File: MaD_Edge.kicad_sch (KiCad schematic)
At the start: 15 parts

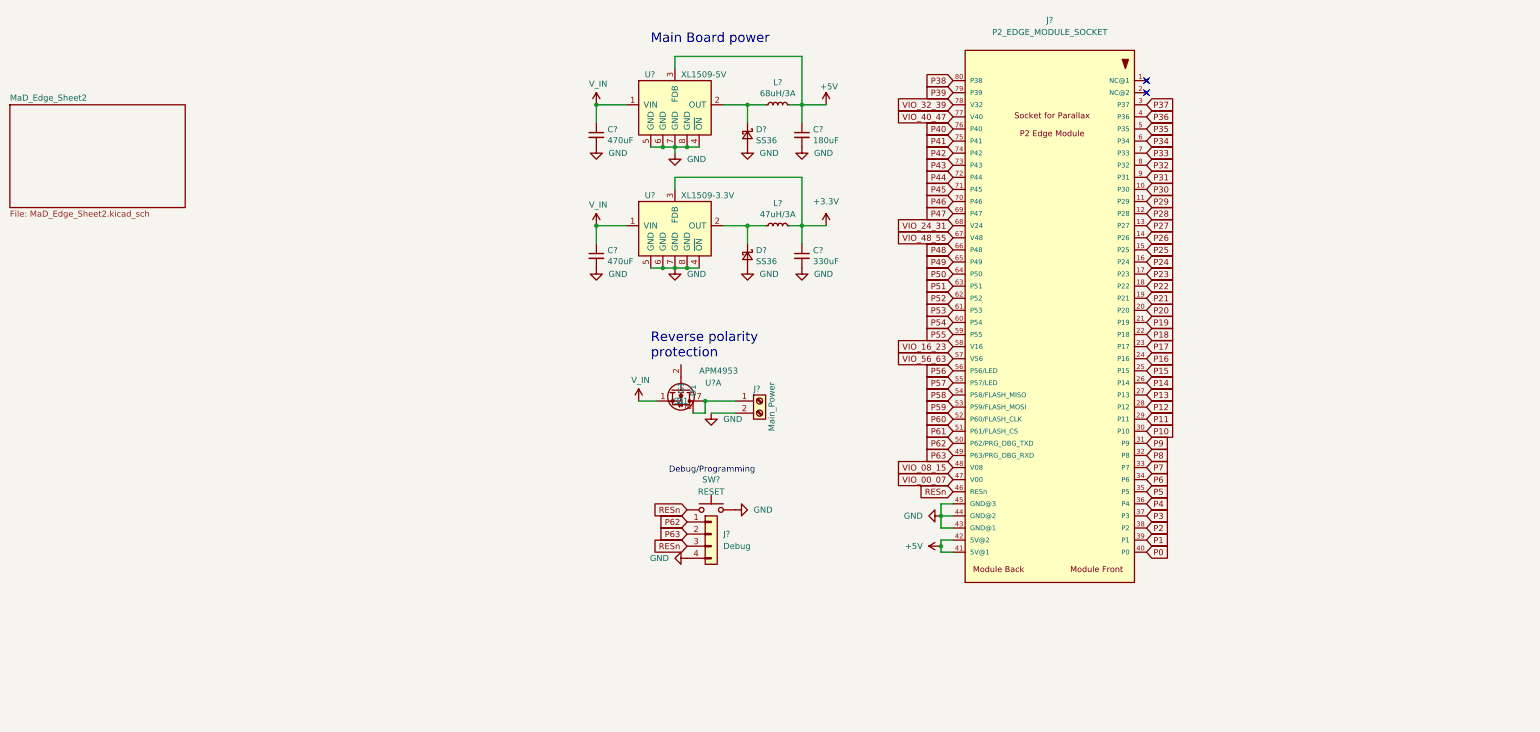
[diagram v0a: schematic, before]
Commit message: new Mad Edge being manufactured
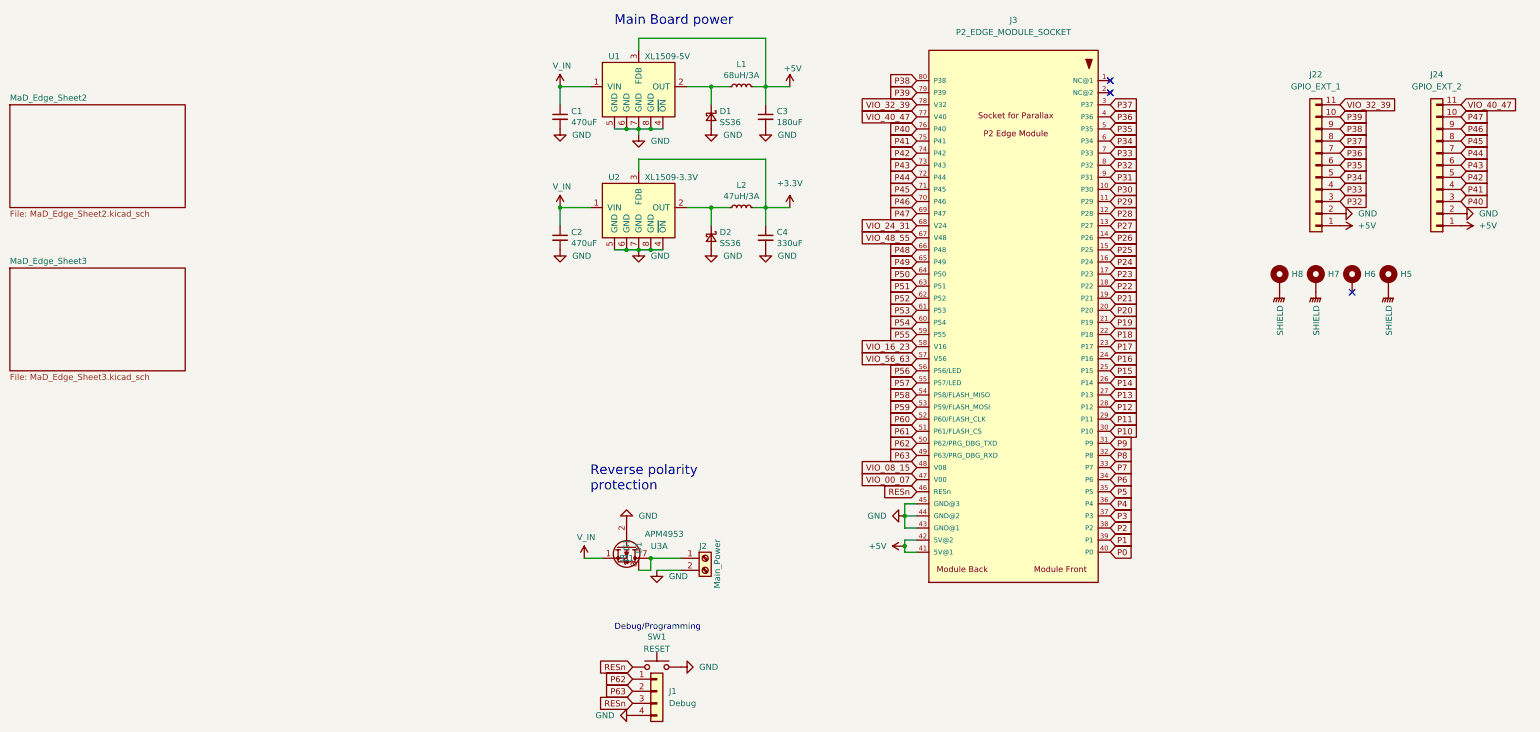
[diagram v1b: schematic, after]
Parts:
- added H5, H6, H7, H8: MountingHole_Pad, MountingHole:MountingHole_4mm_Pad, symbol Mechanical:MountingHole_Pad
- added J22: GPIO_EXT_1, Connector_PinHeader_1.27mm:PinHeader_1x11_P1.27mm_Vertical, symbol Connector_Generic:Conn_01x11
- added J24: GPIO_EXT_2, Connector_PinHeader_1.27mm:PinHeader_1x11_P1.27mm_Vertical, symbol Connector_Generic:Conn_01x11
- C1, C2: renamed from C?; footprint (none) -> Capacitor_SMD:C_Elec_10x10.2; DIGIKEY 399-18277-1-ND -> 10-EEH-ZS1E471PCT-ND; Height (none) -> 12.80mm; LCSC (none) -> C3350; MANUFACTURER (none) -> Panasonic Electronic Components; Manufacturer_Part_Number (none) -> EEH-ZS1E471P; Type NA -> (none); manufacturer_1 (none) -> Honor Elec; manufacturer_part_number_1 (none) -> RVT1V471M1010
- C3: renamed from C?; footprint (none) -> Capacitor_SMD:CP_Elec_8x6.9; DIGIKEY 1189-2158-ND -> P16510CT-ND; Height (none) -> 12.00mm; LCSC (none) -> C413657; MANUFACTURER (none) -> Panasonic Electronic Components; Manufacturer_Part_Number (none) -> 25SVPF180M; Type NA -> (none); manufacturer_1 (none) -> PANASONIC; manufacturer_part_number_1 (none) -> EEEFKE181XSP
- C4: renamed from C?; footprint (none) -> Capacitor_SMD:C_Elec_10x10.2; DIGIKEY 493-11736-1-ND -> P16512CT-ND; Height (none) -> 12.70mm; LCSC (none) -> C5155335; MANUFACTURER (none) -> Panasonic Electronic Components; Manufacturer_Part_Number (none) -> 25SVPF330M; Type NA -> (none); manufacturer_1 (none) -> KNSCHA; manufacturer_part_number_1 (none) -> LZ330UF35V90RV0141
- D1, D2: renamed from D?; footprint (none) -> Diode_SMD:D_SMC; DIGIKEY (none) -> SS36-E3/57TGICT-ND; MANUFACTURER (none) -> Vishay General Semiconductor - Diodes Division; Manufacturer_Part_Number (none) -> SS36-E3/57T; Type BASIC -> (none); manufacturer_1 (none) -> Vishay Intertech; manufacturer_part_number_1 (none) -> SS36-E3/57T
- J1: renamed from J?; footprint (none) -> Connector_PinHeader_2.54mm:PinHeader_1x04_P2.54mm_Vertical; LCSC (none) -> DNP; MANUFACTURER (none) -> DNP; Manufacturer_Part_Number (none) -> DNP; manufacturer_1 (none) -> DNP; manufacturer_part_number_1 (none) -> DNP
- J2: renamed from J?; footprint TerminalBlock:TerminalBlock_bornier-2_P5.08mm -> 70553-0106:705530106; DIGIKEY (none) -> WM4153-ND; LCSC (none) -> C239384; MANUFACTURER (none) -> Molex; Manufacturer_Part_Number (none) -> 0705530106; Type NA -> (none); manufacturer_1 (none) -> CJT(Changjiang Connectors); manufacturer_part_number_1 (none) -> A2547WR-2P
- J3: renamed from J?; footprint P2_EDGE_MODULE_SOCKET:Card_Edge_TH_VERT_1.27mm_80p -> P2_EDGE_MODULE_SOCKET:Card_Edge_SMT_VERT_1.27mm_80p; LCSC (none) -> DNP; Manufacturer_Part_Number (none) -> 450-00309; manufacturer_1 (none) -> DNP; manufacturer_part_number_1 (none) -> DNP
- L1: renamed from L?; footprint (none) -> Inductor_SMD:L_10.4x10.4_H4.8; DIGIKEY (none) -> SRP1038A-470MCT-ND; Height (none) -> 4.00mm; LCSC C497902 -> C408492; MANUFACTURER (none) -> Bourns Inc.; Manufacturer_Part_Number (none) -> SRP1038A-470M; Type EXT -> (none); manufacturer_1 (none) -> Sunlord; manufacturer_part_number_1 (none) -> MWSA1004S-680MT
- L2: renamed from L?; footprint (none) -> Inductor_SMD:L_10.4x10.4_H4.8; LCSC C115409 -> C149548; MANUFACTURER (none) -> Sunltech Tech; Manufacturer_Part_Number (none) -> SLO1365H470MTT; Type EXT -> (none); manufacturer_1 (none) -> SXN(Shun Xiang Nuo Elec); manufacturer_part_number_1 (none) -> SMMS1050-470M
- SW1: renamed from SW?; footprint (none) -> Button_Switch_SMD:SW_SPST_PTS645; LCSC (none) -> C2804591; manufacturer_1 (none) -> C&K; manufacturer_part_number_1 (none) -> PTS645VK31LFS
- U1: renamed from U?; footprint (none) -> Package_SO:SOP-8_3.9x4.9mm_P1.27mm; MANUFACTURER (none) -> XLSEMI; Manufacturer_Part_Number (none) -> XL1509-5.0E1; Type BASIC -> (none); manufacturer_1 (none) -> XLSEMI; manufacturer_part_number_1 (none) -> XL1509-5.0E1
- U2: renamed from U?; footprint (none) -> Package_SO:SOP-8_3.9x4.9mm_P1.27mm; LCSC C74193 -> C74193; MANUFACTURER (none) -> XLSEMI; Manufacturer_Part_Number (none) -> XL1509-3.3E1; Type EXT -> (none); manufacturer_1 (none) -> XLSEMI; manufacturer_part_number_1 (none) -> XL1509-3.3E1
- U3: renamed from U?; MANUFACTURER (none) -> Anpec Elec; Manufacturer_Part_Number (none) -> APM4953KC-TRG; Type BASIC -> (none); manufacturer_1 (none) -> Anpec Elec; manufacturer_part_number_1 (none) -> APM4953KC-TRG
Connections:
- net +5V: now also J22.1 (Pin_1), J24.1 (Pin_1)
- net GND: now also U3.2 (G1), J22.2 (Pin_2), J24.2 (Pin_2)
- net P32: now also J22.3 (Pin_3)
- net P33: now also J22.4 (Pin_4)
- net P34: now also J22.5 (Pin_5)
- net P35: now also J22.6 (Pin_6)
- net P36: now also J22.7 (Pin_7)
- net P37: now also J22.8 (Pin_8)
- net P38: now also J22.9 (Pin_9)
- net P39: now also J22.10 (Pin_10)
- net P40: now also J24.3 (Pin_3)
- net P41: now also J24.4 (Pin_4)
- net P42: now also J24.5 (Pin_5)
- net P43: now also J24.6 (Pin_6)
- net P44: now also J24.7 (Pin_7)
- net P45: now also J24.8 (Pin_8)
- net P46: now also J24.9 (Pin_9)
- net P47: now also J24.10 (Pin_10)
- net VIO_32_39: now also J22.11 (Pin_11)
- net VIO_40_47: now also J24.11 (Pin_11)
- new net SHIELD: H5.1, H7.1, H8.1
- no-connect marks 2 -> 3
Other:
- added sheet MaD_Edge_Sheet3 (MaD_Edge_Sheet3.kicad_sch)
- moved on the sheet: C1, C2, C3, C4, D1, D2, J1, J2, J3, L1, L2, SW1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

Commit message: working version for getting basic data for the thesis
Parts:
- C1, C2, D1, D2: Qty Bought (none) -> 10 - lcsc
- C3, C4, L2, U1, U2, U3: Qty Bought (none) -> 5 - lcsc
- H5, H6, H7, H8, J1, J22, J24, J3, SW1: Qty Bought (none) -> NA
- J2: LCSC C239384 -> C5333422; Qty Bought (none) -> 4 - lcsc
- L1: Qty Bought (none) -> 5 -lcsc
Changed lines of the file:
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@@
       (effects (font (size 1.27 1.27)) hide)
     )
-    (property "LCSC" "C239384" (at 107.95 142.24 0)
+    (property "LCSC" "C5333422" (at 107.95 142.24 0)
       (effects (font (size 1.27 1.27)) hide)
     )
@@
     )
     (property "manufacturer_part_number_1" "A2547WR-2P" (at 107.95 142.24 0)
+      (effects (font (size 1.27 1.27)) hide)
+    )
+    (property "Qty Bought" "4 - lcsc" (at 107.95 142.24 0)
+      (effects (font (size 1.27 1.27)) hide)
+    )
+    (property "Receptical" "" (at 107.95 142.24 0)
       (effects (font (size 1.27 1.27)) hide)
     )
@@
       (effects (font (size 1.27 1.27)) hide)
     )
+    (property "Qty Bought" "NA" (at 251.46 83.82 0)
+      (effects (font (size 1.27 1.27)) hide)
+    )
+    (property "Receptical" "" (at 251.46 83.82 0)
+      (effects (font (size 1.27 1.27)) hide)
+    )
     (pin "1")
     (instances
@@
       (effects (font (size 1.27 1.27)) hide)
     )
+    (property "Qty Bought" "NA" (at 228.6 83.82 0)
+      (effects (font (size 1.27 1.27)) hide)
+    )
+    (property "Receptical" "" (at 228.6 83.82 0)
+      (effects (font (size 1.27 1.27)) hide)
+    )
     (pin "1")
     (instances
@@
       (effects (font (size 1.27 1.27)) hide)
     )
+    (property "Qty Bought" "5 -lcsc" (at 115.57 43.18 0)
+      (effects (font (size 1.27 1.27)) hide)
+    )
+    (property "Receptical" "" (at 115.57 43.18 0)
+      (effects (font (size 1.27 1.27)) hide)
+    )
     (pin "1")
     (pin "2")
@@
     )
     (property "manufacturer_part_number_1" "DNP" (at 97.79 170.18 0)
+      (effects (font (size 1.27 1.27)) hide)
+    )
+    (property "Qty Bought" "NA" (at 97.79 170.18 0)
+      (effects (font (size 1.27 1.27)) hide)
+    )
+    (property "Receptical" "" (at 97.79 170.18 0)
       (effects (font (size 1.27 1.27)) hide)
     )
@@
       (effects (font (size 1.27 1.27)) hide)
     )
+    (property "Qty Bought" "10 - lcsc" (at 77.47 74.93 0)
+      (effects (font (size 1.27 1.27)) hide)
+    )
+    (property "Receptical" "" (at 77.47 74.93 0)
+      (effects (font (size 1.27 1.27)) hide)
+    )
     (pin "1")
     (pin "2")
@@
     )
     (property "manufacturer_part_number_1" "XL1509-3.3E1" (at 93.98 68.58 0)
+      (effects (font (size 1.27 1.27)) hide)
+    )
+    (property "Qty Bought" "5 - lcsc" (at 93.98 68.58 0)
+      (effects (font (size 1.27 1.27)) hide)
+    )
+    (property "Receptical" "" (at 93.98 68.58 0)
       (effects (font (size 1.27 1.27)) hide)
     )
@@
       (effects (font (size 1.27 1.27)) hide)
     )
+    (property "Qty Bought" "5  - lcsc" (at 120.65 49.53 0)
+      (effects (font (size 1.27 1.27)) hide)
+    )
+    (property "Receptical" "" (at 120.65 49.53 0)
+      (effects (font (size 1.27 1.27)) hide)
+    )
     (pin "1")
     (pin "2")
@@
       (effects (font (size 1.27 1.27)) hide)
     )
+    (property "Qty Bought" "NA" (at 236.22 83.82 0)
+      (effects (font (size 1.27 1.27)) hide)
+    )
+    (property "Receptical" "" (at 236.22 83.82 0)
+      (effects (font (size 1.27 1.27)) hide)
+    )
     (pin "1")
     (instances
@@
     )
     (property "manufacturer_part_number_1" "APM4953KC-TRG" (at 91.44 142.24 0)
+      (effects (font (size 1.27 1.27)) hide)
+    )
+    (property "Qty Bought" "5 - lcsc" (at 91.44 142.24 0)
+      (effects (font (size 1.27 1.27)) hide)
+    )
+    (property "Receptical" "" (at 91.44 142.24 0)
       (effects (font (size 1.27 1.27)) hide)
     )
@@
       (effects (font (size 1.27 1.27)) hide)
     )
+    (property "Qty Bought" "NA" (at 97.79 165.1 0)
+      (effects (font (size 1.27 1.27)) hide)
+    )
+    (property "Receptical" "" (at 97.79 165.1 0)
+      (effects (font (size 1.27 1.27)) hide)
+    )
     (pin "1")
     (pin "2")
@@
       (effects (font (size 1.27 1.27)) hide)
     )
+    (property "Qty Bought" "5 - lcsc" (at 115.57 68.58 0)
+      (effects (font (size 1.27 1.27)) hide)
+    )
+    (property "Receptical" "" (at 115.57 68.58 0)
+      (effects (font (size 1.27 1.27)) hide)
+    )
     (pin "1")
     (pin "2")
@@
     )
     (property "manufacturer_part_number_1" "RVT1V471M1010" (at 77.47 49.53 0)
+      (effects (font (size 1.27 1.27)) hide)
+    )
+    (property "Qty Bought" "10 - lcsc" (at 77.47 49.53 0)
+      (effects (font (size 1.27 1.27)) hide)
+    )
+    (property "Receptical" "" (at 77.47 49.53 0)
       (effects (font (size 1.27 1.27)) hide)
     )
@@
     )
     (property "manufacturer_part_number_1" "DNP" (at 236.22 59.69 0)
+      (effects (font (size 1.27 1.27)) hide)
+    )
+    (property "Qty Bought" "NA" (at 236.22 59.69 0)
+      (effects (font (size 1.27 1.27)) hide)
+    )
+    (property "Receptical" "" (at 236.22 59.69 0)
       (effects (font (size 1.27 1.27)) hide)
     )
@@
     )
     (property "manufacturer_part_number_1" "DNP" (at 172.72 91.44 0)
+      (effects (font (size 1.27 1.27)) hide)
+    )
+    (property "Qty Bought" "NA" (at 172.72 91.44 0)
+      (effects (font (size 1.27 1.27)) hide)
+    )
+    (property "Receptical" "" (at 172.72 91.44 0)
       (effects (font (size 1.27 1.27)) hide)
     )
@@
       (effects (font (size 1.27 1.27)) hide)
     )
+    (property "Qty Bought" "5 - lcsc" (at 120.65 74.93 0)
+      (effects (font (size 1.27 1.27)) hide)
+    )
+    (property "Receptical" "" (at 120.65 74.93 0)
+      (effects (font (size 1.27 1.27)) hide)
+    )
     (pin "1")
     (pin "2")
@@
     )
     (property "manufacturer_part_number_1" "DNP" (at 261.62 59.69 0)
+      (effects (font (size 1.27 1.27)) hide)
+    )
+    (property "Qty Bought" "NA" (at 261.62 59.69 0)
+      (effects (font (size 1.27 1.27)) hide)
+    )
+    (property "Receptical" "" (at 261.62 59.69 0)
       (effects (font (size 1.27 1.27)) hide)
     )
@@
       (effects (font (size 1.27 1.27)) hide)
     )
+    (property "Qty Bought" "10 - lcsc" (at 109.22 74.93 0)
+      (effects (font (size 1.27 1.27)) hide)
+    )
+    (property "Receptical" "" (at 109.22 74.93 0)
+      (effects (font (size 1.27 1.27)) hide)
+    )
     (pin "1")
     (pin "2")
@@
       (effects (font (size 1.27 1.27)) hide)
     )
+    (property "Qty Bought" "NA" (at 243.84 83.82 0)
+      (effects (font (size 1.27 1.27)) hide)
+    )
+    (property "Receptical" "" (at 243.84 83.82 0)
+      (effects (font (size 1.27 1.27)) hide)
+    )
     (pin "1")
     (instances
@@
     )
     (property "manufacturer_part_number_1" "XL1509-5.0E1" (at 93.98 43.18 0)
+      (effects (font (size 1.27 1.27)) hide)
+    )
+    (property "Qty Bought" "5 - lcsc" (at 93.98 43.18 0)
+      (effects (font (size 1.27 1.27)) hide)
+    )
+    (property "Receptical" "" (at 93.98 43.18 0)
       (effects (font (size 1.27 1.27)) hide)
     )
@@
       (effects (font (size 1.27 1.27)) hide)
     )
+    (property "Qty Bought" "10 - lcsc" (at 109.22 49.53 0)
+      (effects (font (size 1.27 1.27)) hide)
+    )
+    (property "Receptical" "" (at 109.22 49.53 0)
+      (effects (font (size 1.27 1.27)) hide)
+    )
